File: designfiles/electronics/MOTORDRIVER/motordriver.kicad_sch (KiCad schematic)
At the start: 0 parts

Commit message: made clearer foldernames and cleaned up
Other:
- sheet driverIC2 ports: added GPIO0, GPIO1, GPIO2, HALL_U, HALL_W, PWM_I, PWM_U_H, PWM_U_L, PWM_V_H, PWM_V_L, PWM_W_H, PWM_W_L, SPI_CS, STATUS, UART_RX, UART_TX; removed GPIO3, GPIO4, TMC_CS, TMC_RX, TMC_TX
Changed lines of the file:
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@@
-			)
-		)
-		(pin "GPIO3" input
-			(at 166.37 26.67 180)
-			(effects
-				(font
-					(size 1.27 1.27)
-				)
-				(justify left)
-			)
-		)
-		(pin "GPIO4" input
-			(at 166.37 29.21 180)
-			(effects
-				(font
-					(size 1.27 1.27)
-				)
-				(justify left)
-			)
-		)
-		(pin "TMC_CS" input
-			(at 166.37 44.45 180)
-			(effects
-				(font
-					(size 1.27 1.27)
-				)
-				(justify left)
 			)
 		)
@@
 			)
 		)
-		(pin "TMC_RX" input
-			(at 166.37 53.34 180)
-			(effects
-				(font
-					(size 1.27 1.27)
-				)
-				(justify left)
-			)
-		)
-		(pin "TMC_TX" input
-			(at 166.37 50.8 180)
-			(effects
-				(font
-					(size 1.27 1.27)
-				)
-				(justify left)
-			)
-		)
 		(pin "BRAKE" input
 			(at 236.22 52.07 0)
@@
 			)
 		)
+		(pin "PWM_I" input
+			(at 181.61 25.4 90)
+			(effects
+				(font
+					(size 1.27 1.27)
+				)
+				(justify right)
+			)
+		)
+		(pin "GPIO1" input
+			(at 184.15 25.4 90)
+			(effects
+				(font
+					(size 1.27 1.27)
+				)
+				(justify right)
+			)
+		)
+		(pin "GPIO0" input
+			(at 186.69 25.4 90)
+			(effects
+				(font
+					(size 1.27 1.27)
+				)
+				(justify right)
+			)
+		)
+		(pin "GPIO2" input
+			(at 189.23 25.4 90)
+			(effects
+				(font
+					(size 1.27 1.27)
+				)
+				(justify right)
+			)
+		)
+		(pin "HALL_U" input
+			(at 193.04 25.4 90)
+			(effects
+				(font
+					(size 1.27 1.27)
+				)
+				(justify right)
+			)
+		)
+		(pin "HALL_W" input
+			(at 195.58 25.4 90)
+			(effects
+				(font
+					(size 1.27 1.27)
+				)
+				(justify right)
+			)
+		)
+		(pin "PWM_W_L" input
+			(at 198.12 25.4 90)
+			(effects
+				(font
+					(size 1.27 1.27)
+				)
+				(justify right)
+			)
+		)
+		(pin "PWM_W_H" input
+			(at 195.58 58.42 270)
+			(effects
+				(font
+					(size 1.27 1.27)
+				)
+				(justify left)
+			)
+		)
+		(pin "PWM_U_L" input
+			(at 198.12 58.42 270)
+			(effects
+				(font
+					(size 1.27 1.27)
+				)
+				(justify left)
+			)
+		)
+		(pin "PWM_V_H" input
+			(at 200.66 58.42 270)
+			(effects
+				(font
+					(size 1.27 1.27)
+				)
+				(justify left)
+			)
+		)
+		(pin "PWM_V_L" input
+			(at 203.2 58.42 270)
+			(effects
+				(font
+					(size 1.27 1.27)
+				)
+				(justify left)
+			)
+		)
+		(pin "PWM_U_H" input
+			(at 205.74 58.42 270)
+			(effects
+				(font
+					(size 1.27 1.27)
+				)
+				(justify left)
+			)
+		)
+		(pin "UART_TX" input
+			(at 209.55 58.42 270)
+			(effects
+				(font
+					(size 1.27 1.27)
+				)
+				(justify left)
+			)
+		)
+		(pin "STATUS" input
+			(at 212.09 58.42 270)
+			(effects
+				(font
+					(size 1.27 1.27)
+				)
+				(justify left)
+			)
+		)
+		(pin "UART_RX" input
+			(at 214.63 58.42 270)
+			(effects
+				(font
+					(size 1.27 1.27)
+				)
+				(justify left)
+			)
+		)
+		(pin "SPI_CS" input
+			(at 217.17 58.42 270)
+			(effects
+				(font
+					(size 1.27 1.27)
+				)
+				(justify left)
+			)
+		)

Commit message: fixed root folder schematics
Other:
- sheet driverIC renamed servo1
- sheet driverIC1 renamed servo2
- sheet driverIC2 renamed servo3
- removed sheet drivergates
- added sheet drivergates3 (gates.kicad_sch)
- sheet IO ports: added BRAKE1, BRAKE2, BRAKE3; removed SERVO_1_SIGNAL, SERVO_2_SIGNAL, SERVO_3_SIGNAL
- sheet microcontrollers ports: added BRAKE1, BRAKE2, BRAKE3, INT1_IMU1, INT1_IMU2, RX, SCL_IMU1, SCL_IMU2, SDA_IMU1, SDA_IMU2, SERVO1_CS, SERVO1_PWM_I, SERVO1_RX, SERVO1_STATUS, SERVO1_TX, SERVO2_CS, SERVO2_GPIO0, SERVO2_GPIO1, SERVO2_GPIO2, SERVO2_PWM_I, SERVO2_RX, SERVO2_STATUS, SERVO2_TX, SERVO3_CS, SERVO3_PWM_I, SERVO3_RX, SERVO3_STATUS, SERVO3_TX, TX; removed DB_RX, DB_TX, INT1 IMU1, INT1 IMU2, S1_SIG, S2_SIG, S3_SIG, SCL IMU1, SCL IMU2, SDA IMU1, SDA IMU2, TMC_CLK, TMC_CLK1, TMC_CLK2, TMC_DB_RX, TMC_DB_RX1, TMC_DB_RX2, TMC_DB_TX, TMC_DB_TX1, TMC_DB_TX2, TMC_ENI, TMC_ENI1, TMC_ENI2, driverIC1_CS, driverIC2_CS, driverIC_CS
- sheet servo1 ports: added GPIO0, GPIO1, GPIO2, HALL_U, HALL_W, PWM_I, PWM_U_H, PWM_U_L, PWM_V_H, PWM_V_L, PWM_W_H, PWM_W_L, SPI_CS, STATUS, UART_RX, UART_TX; removed CLK, ENI, GPIO3, GPIO4, HALL_UX, HALL_WY, PWM_UX1_H, PWM_UX1_L, PWM_VX2_H, PWM_VX2_L, PWM_W1_H, PWM_W1_L, TMC_CS, TMC_RX, TMC_TX
- sheet servo2 ports: added GPIO0, GPIO1, GPIO2, HALL_U, HALL_W, PWM_I, PWM_U_H, PWM_U_L, PWM_V_H, PWM_V_L, PWM_W_H, PWM_W_L, SPI_CS, STATUS, UART_RX, UART_TX; removed CLK, ENI, GPIO3, GPIO4, HALL_UX, HALL_WY, PWM_UX1_H, PWM_UX1_L, PWM_VX2_H, PWM_VX2_L, PWM_W1_H, PWM_W1_L, TMC_CS, TMC_RX, TMC_TX
- sheet servo3 ports: added none; removed CLK, ENI, HALL_UX, HALL_WY, PWM_UX1_H, PWM_UX1_L, PWM_VX2_H, PWM_VX2_L, PWM_W1_H, PWM_W1_L
- note added: "why is gpio from tmc -> mc?"

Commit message: small tweaks
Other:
- sheet IO ports: added RESETN; removed none
- sheet servo1: file driverIC.kicad_sch -> servocontroller.kicad_sch
- sheet servo2: file driverIC.kicad_sch -> servocontroller.kicad_sch
- sheet servo3: file driverIC.kicad_sch -> servocontroller.kicad_sch
- note removed: "why is gpio from tmc -> mc?"
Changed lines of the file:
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@@
+	(wire
+		(pts
+			(xy 33.02 83.82) (xy 72.39 83.82)
+		)
+		(stroke
+			(width 0)
+			(type default)
+		)
+	)
 	(wire
 		(pts
@@
 		)
 	)
-	(text "why is gpio from \ntmc -> mc?\n"
-		(exclude_from_sim no)
-		(at 155.194 93.98 0)
-		(effects
-			(font
-				(size 1.27 1.27)
-			)
-		)
-	)
 	(text "Main\nMotors IO"
 		(exclude_from_sim no)
@@
 			)
 		)
-		(property "Sheetfile" "driverIC.kicad_sch"
+		(property "Sheetfile" "servocontroller.kicad_sch"
 			(at 167.64 159.5084 0)
 			(effects
@@
 			)
 		)
+		(pin "RESETN" input
+			(at 33.02 83.82 0)
+			(effects
+				(font
+					(size 1.27 1.27)
+				)
+				(justify right)
+			)
+		)
 		(instances
 			(project "motordriver"
@@
 			)
 		)
-		(property "Sheetfile" "driverIC.kicad_sch"
+		(property "Sheetfile" "servocontroller.kicad_sch"
 			(at 166.37 59.1784 0)
 			(effects
@@
 		)
 		(pin "RESETN" input
-			(at 88.9 57.15 90)
-			(effects
-				(font
-					(size 1.27 1.27)
-				)
-				(justify right)
+			(at 72.39 83.82 180)
+			(effects
+				(font
+					(size 1.27 1.27)
+				)
+				(justify left)
 			)
 		)
@@
 			)
 		)
-		(property "Sheetfile" "driverIC.kicad_sch"
+		(property "Sheetfile" "servocontroller.kicad_sch"
 			(at 166.37 106.1684 0)
 			(effects

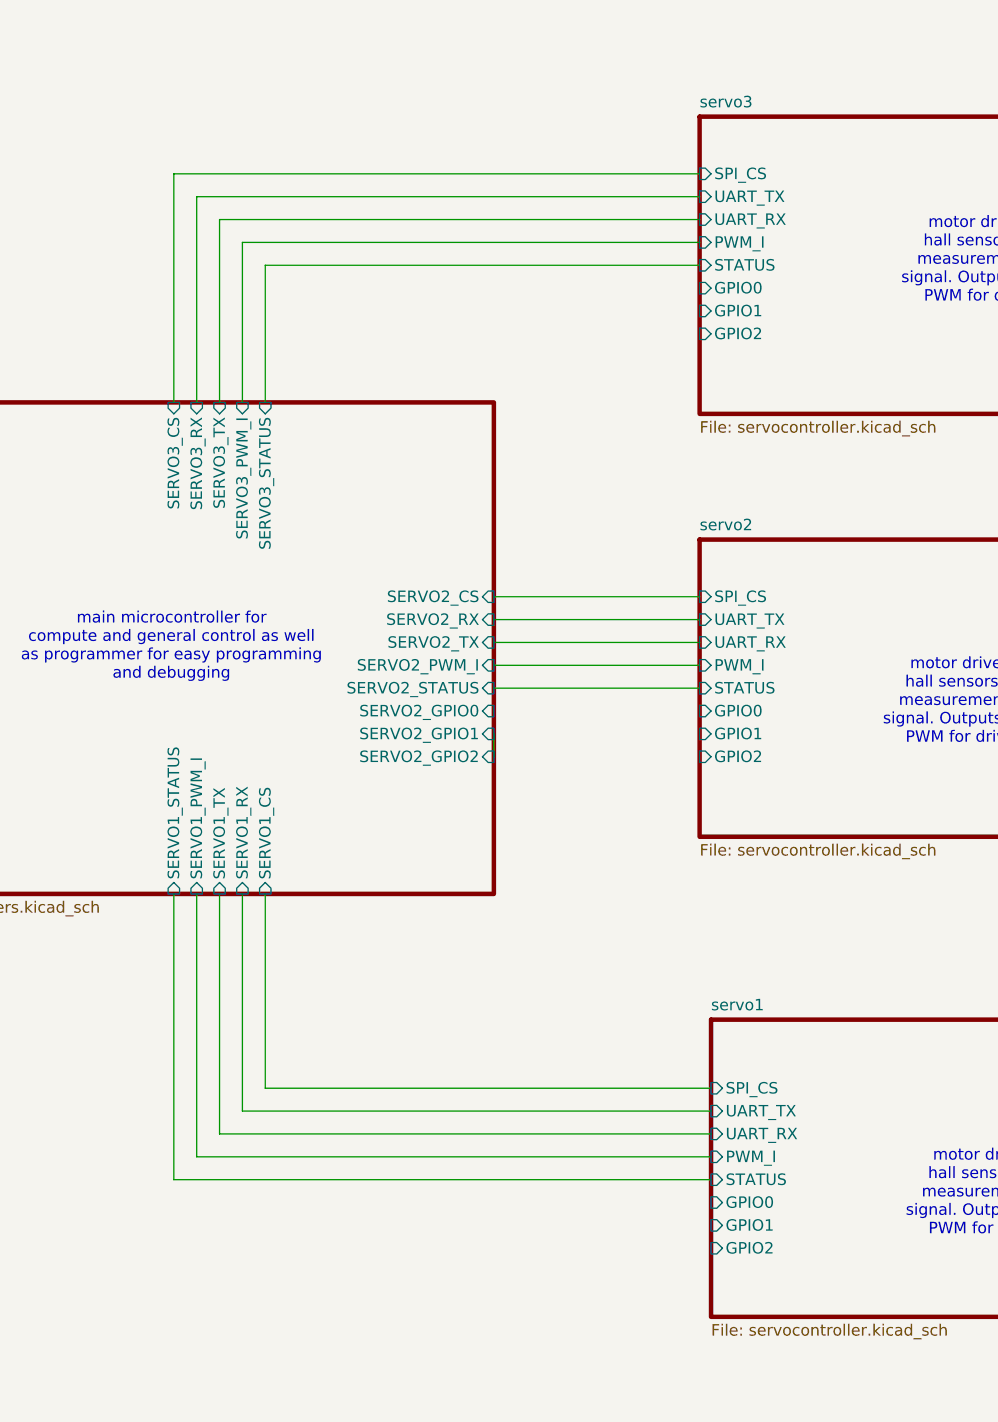
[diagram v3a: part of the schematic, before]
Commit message: tmc gpio pins fixed, spi db fixed, all mcu digital pins fixed, decoupled resetn
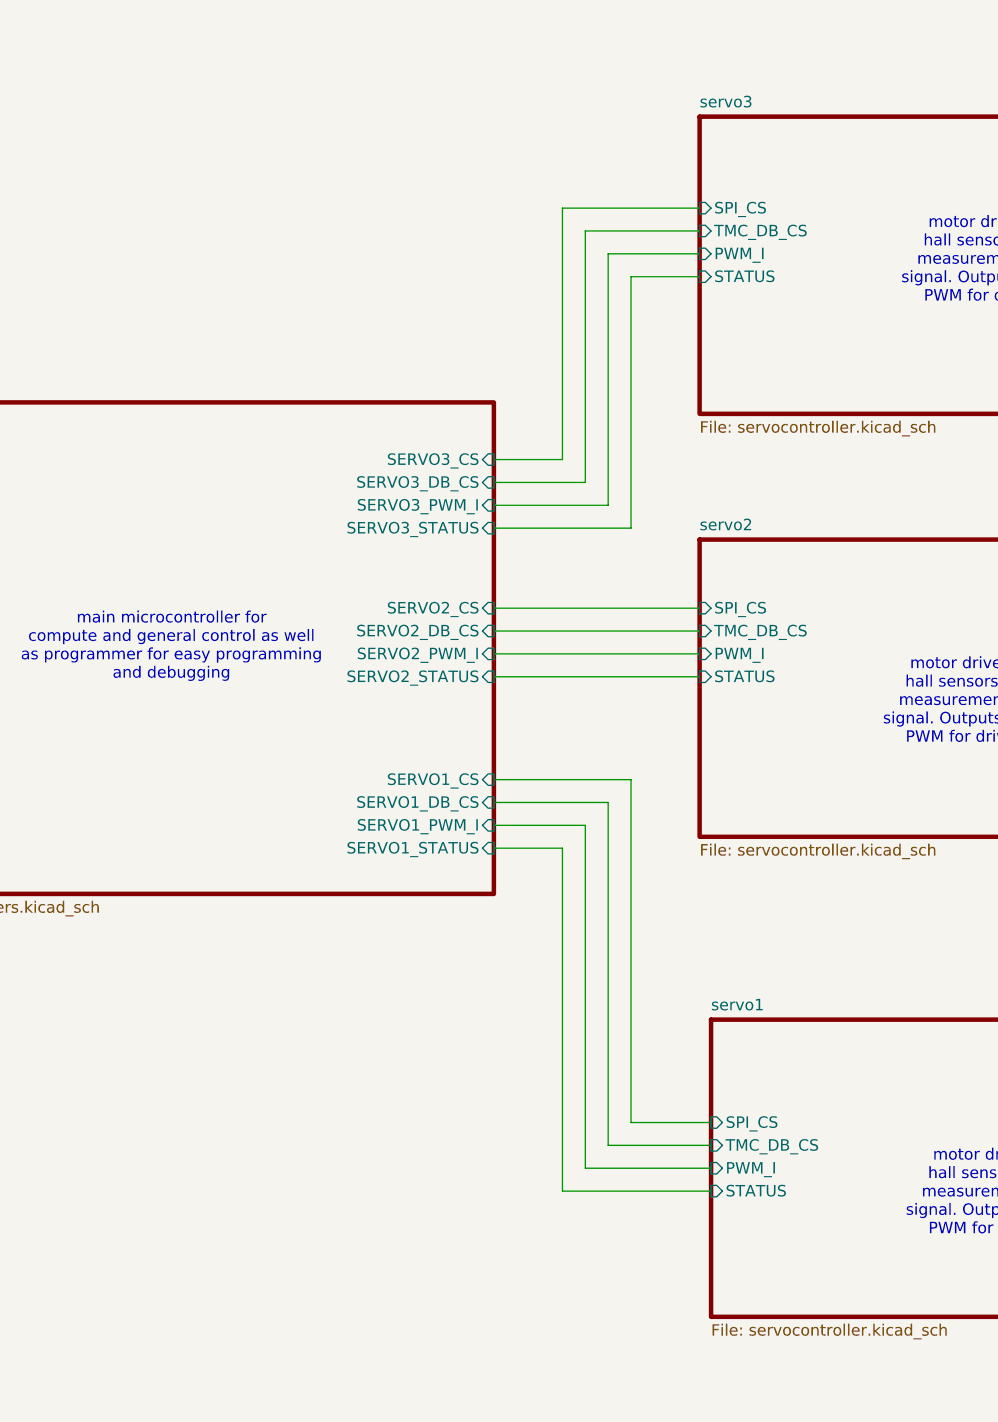
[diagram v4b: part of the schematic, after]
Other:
- sheet microcontrollers ports: added SERVO1_DB_CS, SERVO2_DB_CS, SERVO3_DB_CS; removed SERVO1_RX, SERVO1_TX, SERVO2_GPIO0, SERVO2_GPIO1, SERVO2_GPIO2, SERVO2_RX, SERVO2_TX, SERVO3_RX, SERVO3_TX
- sheet servo1 ports: added TMC_DB_CS; removed GPIO0, GPIO1, GPIO2, UART_RX, UART_TX
- sheet servo2 ports: added TMC_DB_CS; removed GPIO0, GPIO1, GPIO2, UART_RX, UART_TX
- sheet servo3 ports: added TMC_DB_CS; removed GPIO0, GPIO1, GPIO2, UART_RX, UART_TX

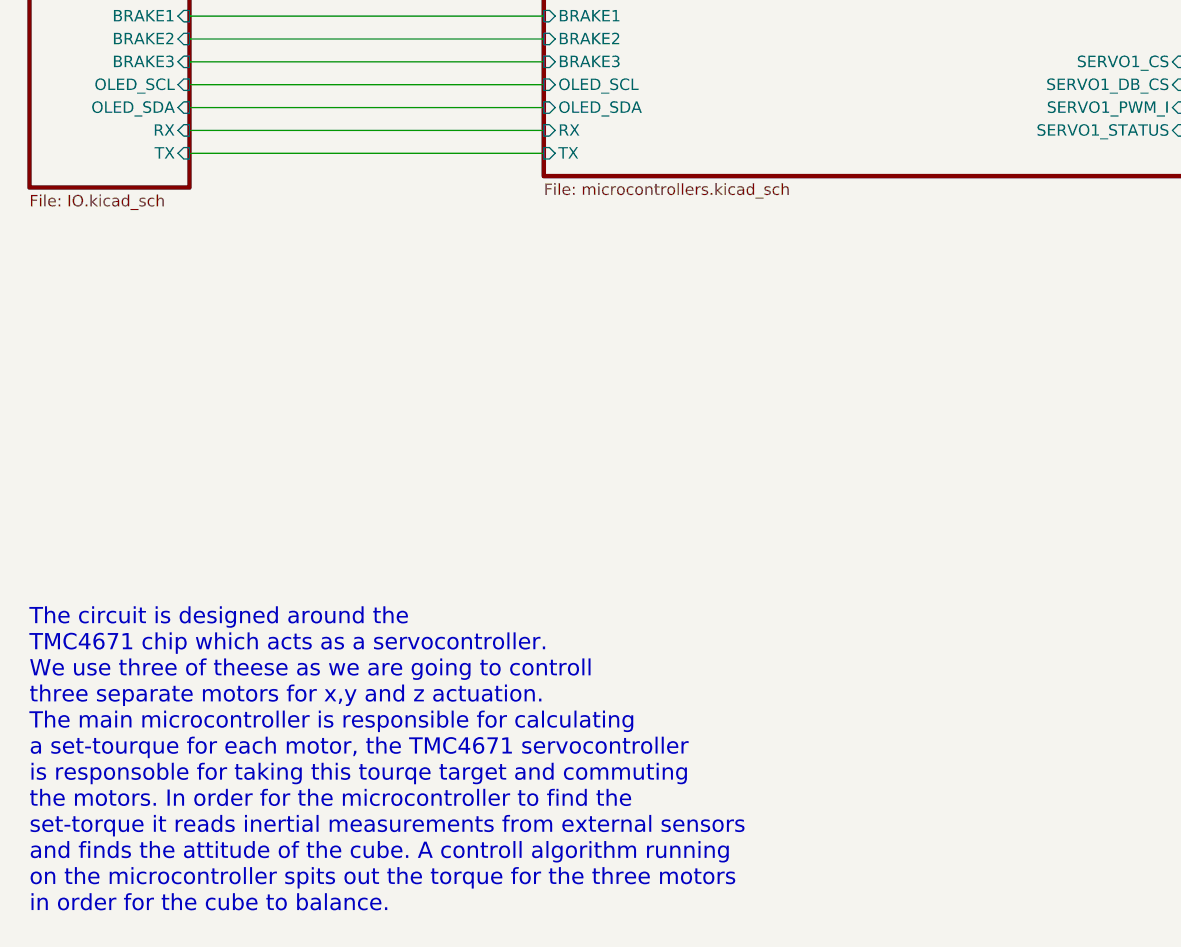
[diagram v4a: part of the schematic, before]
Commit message: double checked SERCOM again, as well as PWM and interrupt pin capabilities
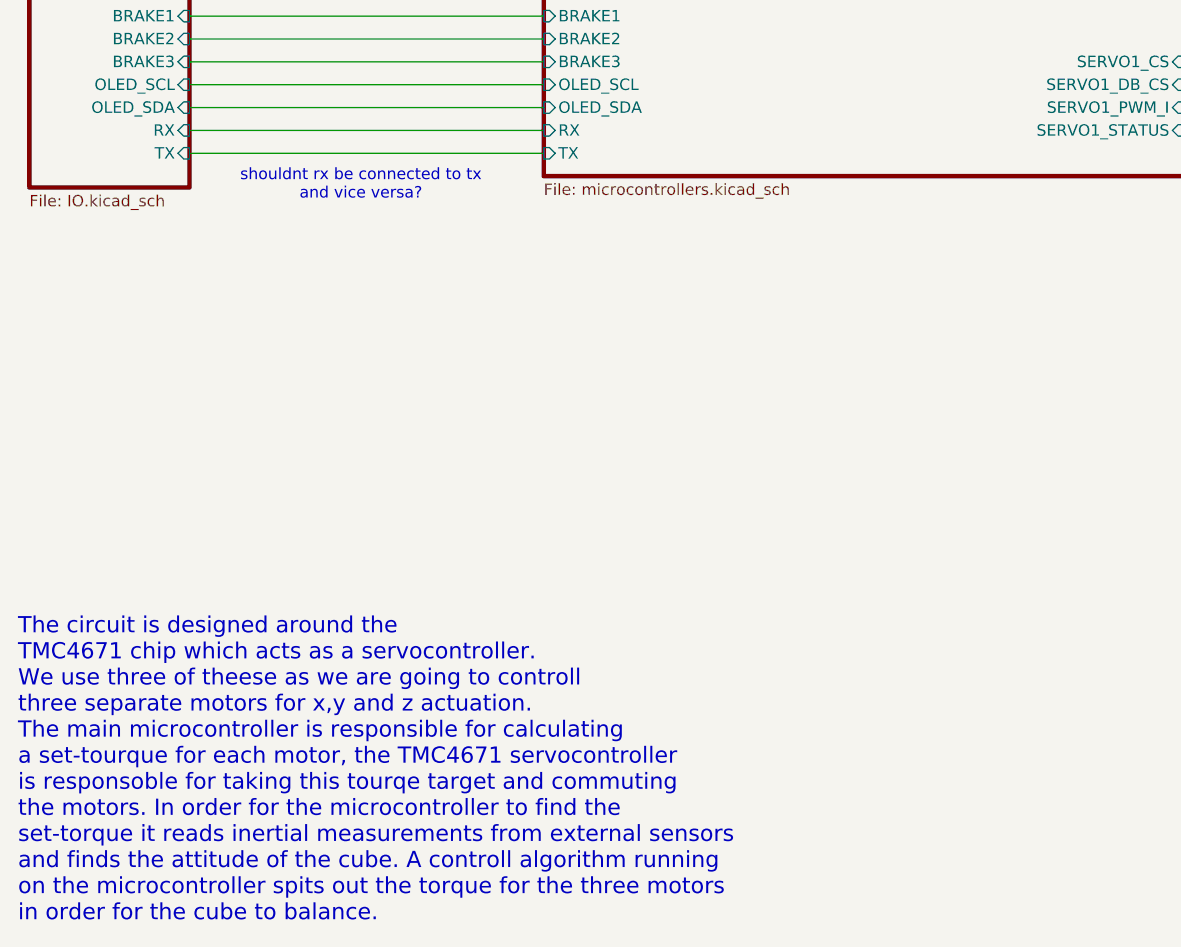
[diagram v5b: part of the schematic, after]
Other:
- note added: "shouldnt rx be connected to tx and vice versa?"
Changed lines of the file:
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@@
+		)
+	)
+	(text "shouldnt rx be connected to tx\nand vice versa?"
+		(exclude_from_sim no)
+		(at 52.07 112.776 0)
+		(effects
+			(font
+				(size 1.27 1.27)
+			)
 		)
 	)
@@
 	(text "The circuit is designed around the\nTMC4671 chip which acts as a servocontroller.\nWe use three of theese as we are going to controll\nthree separate motors for x,y and z actuation.\nThe main microcontroller is responsible for calculating\na set-tourque for each motor, the TMC4671 servocontroller\nis responsoble for taking this tourqe target and commuting\nthe motors. In order for the microcontroller to find the\nset-torque it reads inertial measurements from external sensors\nand finds the attitude of the cube. A controll algorithm running\non the microcontroller spits out the torque for the three motors\nin order for the cube to balance."
 		(exclude_from_sim no)
-		(at 15.24 176.784 0)
+		(at 13.97 177.8 0)
 		(effects
 			(font

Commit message: worked on PCB
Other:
- sheet IO ports: added INT_IMU1, INT_IMU2, INT_IMU3, SCL_IMU1, SCL_IMU2, SCL_IMU3, SDA_IMU1, SDA_IMU2, SDA_IMU3; removed INT1 IMU1, INT1 IMU2, SCL IMU1, SCL IMU2, SDA IMU1, SDA IMU2
- sheet microcontrollers ports: added INT_IMU1, INT_IMU2, INT_IMU3, SCL_IMU3, SDA_IMU3; removed INT1_IMU1, INT1_IMU2
- note removed: "shouldnt rx be connected to tx and vice versa?"

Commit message: worked on PCB
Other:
- sheet IO ports: added none; removed INT_IMU3, SCL_IMU3, SDA_IMU3
- sheet microcontrollers ports: added none; removed INT_IMU3, SCL_IMU3, SDA_IMU3
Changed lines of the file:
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@@
-	(wire
-		(pts
-			(xy 33.02 76.2) (xy 72.39 76.2)
-		)
-		(stroke
-			(width 0)
-			(type default)
-		)
-	)
 	(wire
 		(pts
@@
 	(wire
 		(pts
-			(xy 33.02 78.74) (xy 72.39 78.74)
-		)
-		(stroke
-			(width 0)
-			(type default)
-		)
-	)
-	(wire
-		(pts
 			(xy 205.74 16.51) (xy 205.74 25.4)
 		)
@@
 		(pts
 			(xy 236.22 137.16) (xy 242.57 137.16)
-		)
-		(stroke
-			(width 0)
-			(type default)
-		)
-	)
-	(wire
-		(pts
-			(xy 33.02 73.66) (xy 72.39 73.66)
 		)
 		(stroke
@@
 			)
 		)
-		(pin "SDA_IMU3" input
-			(at 33.02 76.2 0)
-			(effects
-				(font
-					(size 1.27 1.27)
-				)
-				(justify right)
-			)
-		)
-		(pin "SCL_IMU3" input
-			(at 33.02 73.66 0)
-			(effects
-				(font
-					(size 1.27 1.27)
-				)
-				(justify right)
-			)
-		)
-		(pin "INT_IMU3" input
-			(at 33.02 78.74 0)
-			(effects
-				(font
-					(size 1.27 1.27)
-				)
-				(justify right)
-			)
-		)
 		(pin "SCL_IMU2" input
 			(at 33.02 66.04 0)
@@
 			)
 		)
-		(pin "INT_IMU3" input
-			(at 72.39 78.74 180)
-			(effects
-				(font
-					(size 1.27 1.27)
-				)
-				(justify left)
-			)
-		)
 		(pin "INT_IMU2" input
 			(at 72.39 71.12 180)
@@
 			(effects
 				(font
-					(size 1.27 1.27)
-				)
-				(justify left)
-			)
-		)
-		(pin "SDA_IMU3" input
-			(at 72.39 76.2 180)
-			(effects
-				(font
-					(size 1.27 1.27)
-				)
-				(justify left)
-			)
-		)
-		(pin "SCL_IMU3" input
-			(at 72.39 73.66 180)
-			(effects
-				(font
